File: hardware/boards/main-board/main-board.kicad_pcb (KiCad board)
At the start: 4 copper layers, 292.4 x 42 mm, 159 parts, among them J1 2x12 1.27mm shrouded box head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, J2 1x3, J4 12-way, J5 12-way, J6 8-way 2.54mm right-angle pin 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, Q1 AO3401A, SW1 KS-33, SW2 KS-33, SW3 KS-33, SW4 KS-33, SW5 KS-33, SW6 KS-33, SW7 KS-33, SW8 KS-33, U1 SP0504BAHT or equivalent 4-ch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, U10 MPXV4006DP, U11 SP0504BAHTG 4-channel 5V array, U2 MCP3202-CI/SN, U3 OPA2197IDR, U4 REF5050IDR, U5 R-78E5.0-1.0, U6 74AHCT125, U7 74HCS165, U8 74HCS165, U9 SP0504BAHTG 4-channel 5V array

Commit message: #35 pass 2: values — C1 18nF C0G/NP0, D5/D6 PESD12VL1BA to match the sheets
Owner, 2026-10-04, in the working chat: "Yes, go ahead". Footprints unchanged,
no copper moved; pcb.py check 0 errors (the three parity errors cleared).

Gate-Red: known red, not this commit's: 37 deferred cad outputs, the module-iso coverage row (sim), module-main's kicad check; main-board renders/fab stale until the pass's final render

Co-Authored-By: Claude Opus 5.5 <noreply@anthropic.com>
Claude-Session: https://claude.ai/code/session_01LmB4muFXnoLprWX4JzuJ5A
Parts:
- C1: value 47nF C0G/NP0 -> 18nF C0G/NP0
- D5, D6: value PESD12VS1UA or equivalent 12V-standoff ESD diode -> PESD12VL1BA
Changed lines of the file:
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@@
 			)
 		)
-		(property "Value" "47nF C0G/NP0"
+		(property "Value" "18nF C0G/NP0"
 			(at 0 1.68 90)
 			(layer "F.Fab")
@@
 			)
 		)
-		(property "Value" "PESD12VS1UA or equivalent 12V-standoff ESD diode"
+		(property "Value" "PESD12VL1BA"
 			(at 0.1 1.9 90)
 			(layer "F.Fab")
@@
 			)
 		)
-		(property "Value" "PESD12VS1UA or equivalent 12V-standoff ESD diode"
+		(property "Value" "PESD12VL1BA"
 			(at 0.1 1.9 90)
 			(layer "F.Fab")

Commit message: #35 pass 2: R1–R5 — the five proven single-run fixes
R1 CHAIN_SHLD by J5 13.2 -> 11.2 mm; R2 KEY_LT4 hump flattened 14.3 -> 13.0;
R3 LT3 switch leg north of SW3's hole 13.2 -> 12.2; R4 SCLK one straight run
at y 127.1 under D2; R5 IO36 re-laid with one step each end 168.3 -> 166.1.
The reviewer's proven paths (review35 reroute.json), laid locked. Zones filled;
KiCad DRC 0 unconnected / 0 violations; pcb.py check 0 errors.

Gate-Red: known red, not this commit's: 37 deferred cad outputs, the module-iso coverage row (sim), module-main's kicad check; main-board renders/fab stale until the pass's final render

Co-Authored-By: Claude Opus 5.5 <noreply@anthropic.com>
Claude-Session: https://claude.ai/code/session_01LmB4muFXnoLprWX4JzuJ5A
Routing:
- net /IO36: track 265.1 -> 262.9 mm
- net /CHAIN_SHLD: track 263.1 -> 261.1 mm
- net /KEY_LT4: track 51.4 -> 50.1 mm
- net /LT3/SWITCH_LEG: track 13.2 -> 12.2 mm
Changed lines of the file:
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@@
 	)
 	(segment
-		(start 231.1 108.5)
-		(end 231.1 111.9)
-		(width 0.25)
-		(layer "F.Cu")
-		(net 6)
-	)
-	(segment
 		(start 240.5 112.9)
 		(end 245.1 112.9)
@@
 	)
 	(segment
-		(start 231.1 111.9)
-		(end 231.7 112.5)
+		(start 236.1 108.5)
+		(end 240.5 112.9)
 		(width 0.25)
+		(locked yes)
 		(layer "F.Cu")
 		(net 6)
@@
 	)
 	(segment
-		(start 231.7 112.5)
-		(end 240.1 112.5)
+		(start 231.1 108.5)
+		(end 236.1 108.5)
 		(width 0.25)
+		(locked yes)
 		(layer "F.Cu")
 		(net 6)
@@
 		(net 6)
 	)
-	(segment
-		(start 240.1 112.5)
-		(end 240.5 112.9)
-		(width 0.25)
-		(layer "F.Cu")
-		(net 6)
-	)
 	(via
 		(at 124.7 134.1)
@@
 	)
 	(segment
-		(start 176.3 139.5)
-		(end 180.1 135.7)
+		(start 194.5 135.7)
+		(end 158.3 135.7)
 		(width 0.25)
+		(locked yes)
 		(layer "B.Cu")
 		(net 17)
 	)
 	(segment
-		(start 180.1 135.7)
-		(end 210.5 135.7)
+		(start 113.1 139.5)
+		(end 107.3 133.699999)
 		(width 0.25)
+		(locked yes)
 		(layer "B.Cu")
 		(net 17)
 	)
 	(segment
-		(start 214.3 139.5)
-		(end 246.7 139.5)
+		(start 321.9 136.5)
+		(end 321.9 136.3)
 		(width 0.25)
 		(layer "B.Cu")
@@
 	)
 	(segment
-		(start 321.9 136.5)
-		(end 321.9 136.3)
+		(start 107.3 133.699999)
+		(end 104.1 133.699999)
 		(width 0.25)
+		(locked yes)
 		(layer "B.Cu")
 		(net 17)
 	)
 	(segment
-		(start 105.1 134.7)
-		(end 105.1 138.3)
+		(start 154.5 139.5)
+		(end 113.1 139.5)
 		(width 0.25)
+		(locked yes)
 		(layer "B.Cu")
 		(net 17)
 	)
 	(segment
-		(start 105.1 138.3)
-		(end 106.3 139.5)
+		(start 252.1 134.1)
+		(end 247.7 138.5)
 		(width 0.25)
+		(locked yes)
 		(layer "B.Cu")
 		(net 17)
 	)
 	(segment
-		(start 254.9 131.3)
-		(end 254.9 129.9)
+		(start 252.1 132.699999)
+		(end 252.1 134.1)
 		(width 0.25)
+		(locked yes)
 		(layer "B.Cu")
 		(net 17)
 	)
 	(segment
-		(start 106.3 139.5)
-		(end 176.3 139.5)
+		(start 158.3 135.7)
+		(end 154.5 139.5)
 		(width 0.25)
+		(locked yes)
 		(layer "B.Cu")
 		(net 17)
 	)
 	(segment
-		(start 254.9 129.9)
-		(end 258.5 126.3)
+		(start 247.7 138.5)
+		(end 220.1 138.5)
 		(width 0.25)
+		(locked yes)
 		(layer "B.Cu")
 		(net 17)
 	)
 	(segment
-		(start 210.5 135.7)
-		(end 214.3 139.5)
+		(start 258.5 126.3)
+		(end 252.1 132.699999)
 		(width 0.25)
+		(locked yes)
 		(layer "B.Cu")
 		(net 17)
 	)
 	(segment
-		(start 323.5 134.7)
-		(end 334.9 134.7)
+		(start 220.1 138.5)
+		(end 216.5 134.9)
 		(width 0.25)
+		(locked yes)
 		(layer "B.Cu")
 		(net 17)
 	)
 	(segment
-		(start 319.7 126.3)
-		(end 319.7 129.9)
+		(start 216.5 134.9)
+		(end 195.3 134.9)
 		(width 0.25)
+		(locked yes)
 		(layer "B.Cu")
 		(net 17)
 	)
 	(segment
-		(start 104.1 133.699999)
-		(end 105.1 134.7)
+		(start 323.5 134.7)
+		(end 334.9 134.7)
+		(width 0.25)
+		(layer "B.Cu")
+		(net 17)
+	)
+	(segment
+		(start 319.7 126.3)
+		(end 319.7 129.9)
 		(width 0.25)
 		(layer "B.Cu")
@@
 	)
 	(segment
-		(start 246.7 139.5)
-		(end 254.9 131.3)
+		(start 195.3 134.9)
+		(end 194.5 135.7)
 		(width 0.25)
+		(locked yes)
 		(layer "B.Cu")
 		(net 17)
@@
 	)
 	(segment
-		(start 150.1 106.7)
-		(end 149.1 106.7)
+		(start 151.5 108.3)
+		(end 147.5 108.3)
 		(width 0.25)
+		(locked yes)
 		(layer "B.Cu")
 		(net 26)
 	)
 	(segment
-		(start 155.3 111.9)
-		(end 150.1 106.7)
+		(start 155.9 111.9)
+		(end 155.1 111.9)
 		(width 0.25)
+		(locked yes)
 		(layer "B.Cu")
 		(net 26)
 	)
 	(segment
-		(start 155.9 111.9)
-		(end 155.3 111.9)
+		(start 155.1 111.9)
+		(end 151.5 108.3)
 		(width 0.25)
+		(locked yes)
 		(layer "B.Cu")
 		(net 26)
 	)
 	(segment
-		(start 139.9 113.9)
-		(end 137.1 116.7)
+		(start 147.5 108.3)
+		(end 145.3 110.5)
 		(width 0.25)
+		(locked yes)
 		(layer "B.Cu")
 		(net 26)
 	)
 	(segment
-		(start 149.1 106.7)
-		(end 145.3 110.5)
+		(start 139.9 113.9)
+		(end 137.1 116.7)
 		(width 0.25)
 		(layer "B.Cu")
@@
 	)
 	(segment
-		(start 145.299999 139.5)
-		(end 150.3 139.5)
+		(start 150.9 134.9)
+		(end 152.9 136.9)
 		(width 0.25)
+		(locked yes)
 		(layer "F.Cu")
 		(net 35)
 	)
 	(segment
-		(start 142.1 136.3)
-		(end 145.299999 139.5)
+		(start 144.9 136.3)
+		(end 146.3 134.9)
 		(width 0.25)
+		(locked yes)
 		(layer "F.Cu")
 		(net 35)
 	)
 	(segment
-		(start 150.3 139.5)
-		(end 152.9 136.9)
+		(start 146.3 134.9)
+		(end 150.9 134.9)
 		(width 0.25)
+		(locked yes)
+		(layer "F.Cu")
+		(net 35)
+	)
+	(segment
+		(start 142.1 136.3)
+		(end 144.9 136.3)
+		(width 0.25)
+		(locked yes)
 		(layer "F.Cu")
 		(net 35)
@@
 	)
 	(segment
-		(start 336.9 126.7)
-		(end 345.5 126.7)
+		(start 354.9 127.1)
+		(end 338.1 127.1)
 		(width 0.25)
+		(locked yes)
 		(layer "B.Cu")
 		(net 42)
 	)
 	(segment
-		(start 345.9 127.1)
-		(end 354.9 127.1)
+		(start 336.9 126.7)
+		(end 335.5 128.1)
 		(width 0.25)
+		(locked yes)
 		(layer "B.Cu")
 		(net 42)
 	)
 	(segment
-		(start 345.5 126.7)
-		(end 345.9 127.1)
+		(start 337.7 126.7)
+		(end 336.9 126.7)
 		(width 0.25)
+		(locked yes)
 		(layer "B.Cu")
 		(net 42)
 	)
 	(segment
-		(start 335.5 128.1)
-		(end 336.9 126.7)
+		(start 338.1 127.1)
+		(end 337.7 126.7)
 		(width 0.25)
+		(locked yes)
 		(layer "B.Cu")
 		(net 42)

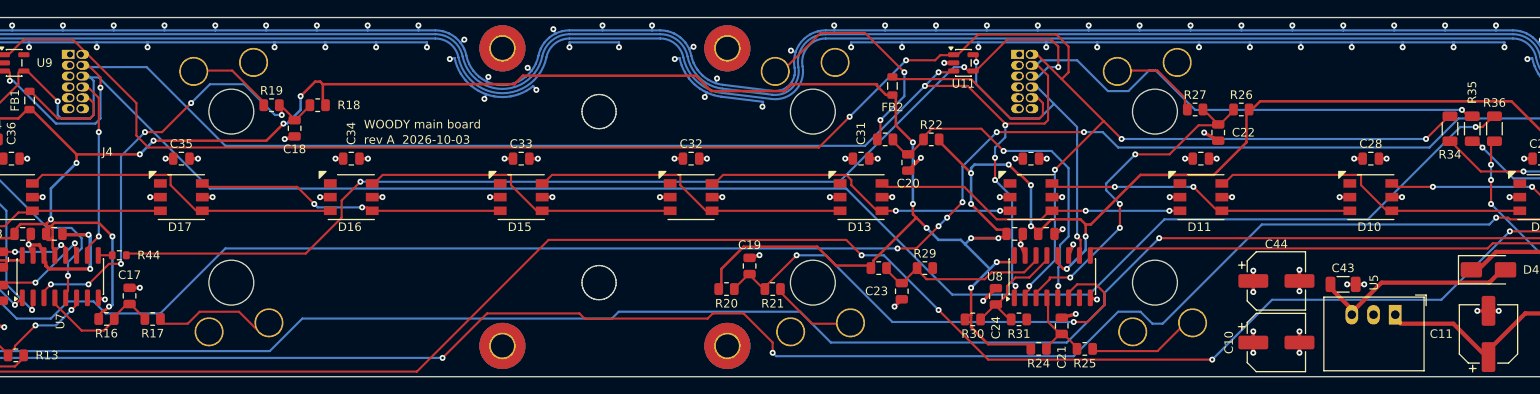
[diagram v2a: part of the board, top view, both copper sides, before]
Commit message: #35 pass 2: R11 WIP — U8/J5 fan-in re-laid (82 -> 72 vias on 14 nets), joins not yet clean
Checkpoint (container restarts). 14 nets re-laid in the U8/J5 box in one pass,
DEV_3V3 first on F, then key lines, chain, IO bus; all new copper locked.
KiCad DRC: 0 unconnected, 0 violations. pcb.py check: 6 errors still to fix
in the next commit (one 0.04 mm dangling stub, five acute joins at cut ends).

Gate-Red: WIP: pcb.py check main-board 6 errors (tracks acid traps, 1 dangling stub) fixed next commit; known red: 37 deferred cad outputs, the module-iso coverage row (sim), module-main's kicad check; main-board renders/fab stale until the final render

Co-Authored-By: Claude Opus 5.5 <noreply@anthropic.com>
Claude-Session: https://claude.ai/code/session_01LmB4muFXnoLprWX4JzuJ5A
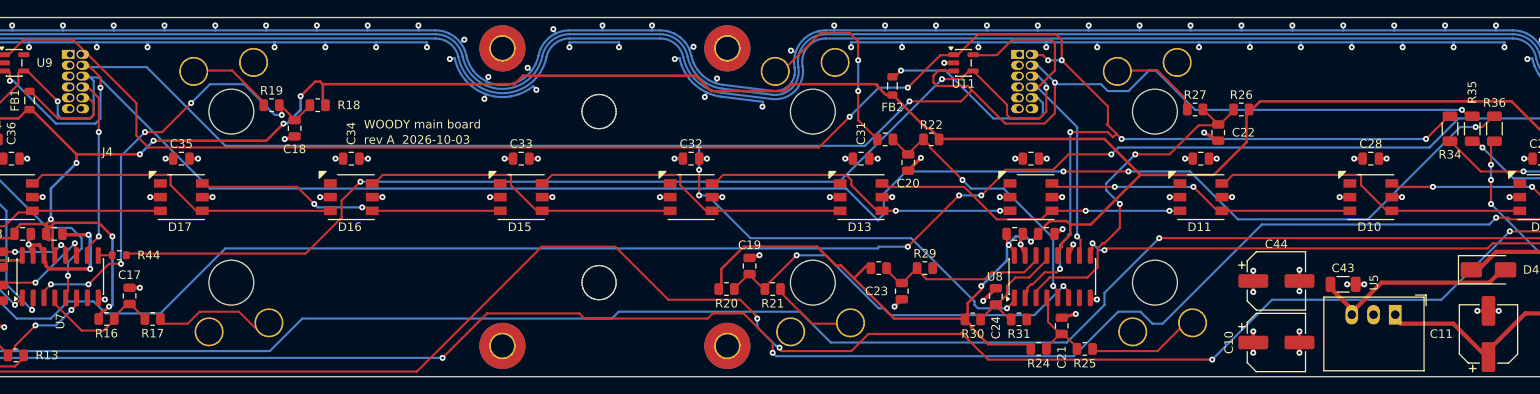
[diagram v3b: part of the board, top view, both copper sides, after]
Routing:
- net /CHAIN_SHLD: track 261.1 -> 291.9 mm, vias 11 -> 10
- net DEV_3V3: track 498.0 -> 483.8 mm, vias 27 -> 16
- net /KEY_RT1: track 53.8 -> 44.8 mm
- net /CHAIN_SCK: track 250.5 -> 255.7 mm, vias 8 -> 10
- net /HOP_RH_RT: track 35.5 -> 40.1 mm, vias 2 -> 1
- net /KEY_RT2: track 36.2 -> 32.4 mm
- net /IO39: track 260.9 -> 257.1 mm, vias 10 -> 8
- net /RT2/SWITCH_LEG: track 25.4 -> 22.6 mm
- net /KEY_RT4: track 36.7 -> 38.8 mm, vias 4 -> 2
- net /V3V3_CHAIN_RH: track 21.5 -> 23.5 mm, vias 0 -> 1
- net /IO35: track 276.8 -> 278.8 mm
- net /CHAIN_QH_RT: track 83.9 -> 85.8 mm, vias 2 -> 4
- net /HOP_LT_RH: track 124.8 -> 126.2 mm
- net /CHAIN_SER_LH: track 203.6 -> 202.5 mm, vias 2 -> 4

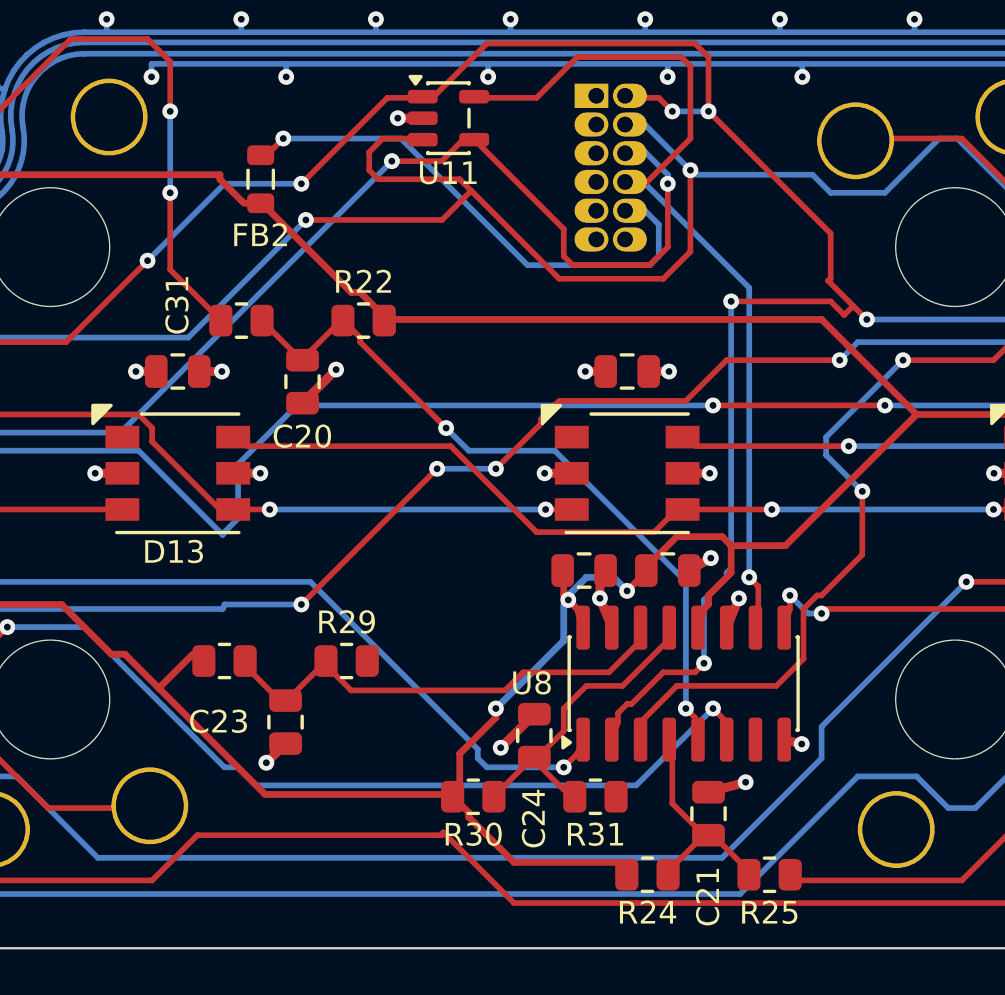
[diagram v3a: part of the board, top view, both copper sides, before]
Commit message: #35 pass 2: R11 (R6–R10, R13 nets, R21) — U8/J5 fan-in re-laid, joins squared
14 nets re-laid together in the U8/J5 box (226,103 - 252,137): DEV_3V3 first,
preferring F, then KEY_RT1/RT2/RT4 and the RT2 leg, the J5/U11 chain (HOP_RH_RT,
HOP_LT_RH, CHAIN_SHLD, CHAIN_SCK, V3V3_CHAIN_RH), CHAIN_QH_RT, CHAIN_SER_LH,
then the IO bus (IO39, IO35); A* on the board's own obstacle model, via cost 60
grid steps, string-pulled to straight and 45-degree runs, all locked. Vias on
those nets 82 -> 72 (board signal vias 148 -> 138), 0 unconnected. The mid-run
via of R21 is gone with DEV_3V3's re-lay. Six joins the re-lay left acute or
doubled squared by hand; pcb_route.tidy run with its locked-via trap guarded.
DRC 0/0; pcb.py check 0 errors.

Gate-Red: known red, not this commit's: 37 deferred cad outputs, the module-iso coverage row (sim), module-main's kicad check; main-board renders/fab stale until the final render

Co-Authored-By: Claude Opus 5.5 <noreply@anthropic.com>
Claude-Session: https://claude.ai/code/session_01LmB4muFXnoLprWX4JzuJ5A
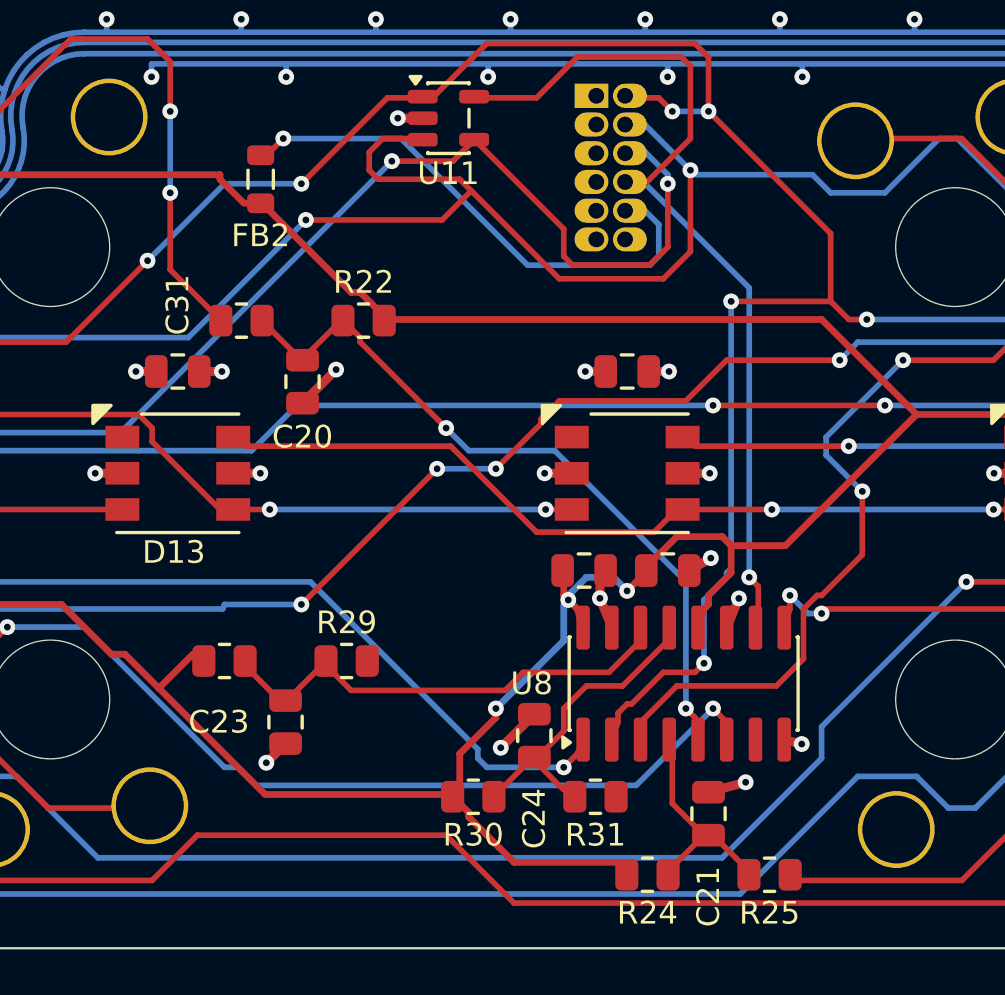
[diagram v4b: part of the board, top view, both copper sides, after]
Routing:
- net /CHAIN_SER_LH: track 202.5 -> 198.0 mm
- net /CHAIN_SCK: track 255.7 -> 254.6 mm
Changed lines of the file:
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@@
 	)
 	(segment
-		(start 243.1 132.1)
-		(end 243.1 132.5)
+		(start 252.5 113.9)
+		(end 253.3 114.7)
 		(width 0.25)
 		(locked yes)
@@
 	)
 	(segment
-		(start 252.375 112.975)
-		(end 252.4 113)
+		(start 243.1 132.1)
+		(end 243.1 132.5)
 		(width 0.25)
 		(locked yes)
@@
 	)
 	(segment
-		(start 243.1 132.5)
-		(end 242.825 133.275)
+		(start 253.3 114.7)
+		(end 254.1 114.7)
 		(width 0.25)
 		(locked yes)
@@
 	)
 	(segment
-		(start 138.9 110.5)
-		(end 138.9 114.3)
+		(start 243.1 132.5)
+		(end 242.825 133.275)
 		(width 0.25)
+		(locked yes)
 		(layer "F.Cu")
 		(net 4)
 	)
 	(segment
-		(start 252.5 112.9)
-		(end 252.4 113)
+		(start 138.9 110.5)
+		(end 138.9 114.3)
 		(width 0.25)
-		(locked yes)
 		(layer "F.Cu")
 		(net 4)
@@
 	)
 	(segment
-		(start 252.4 113)
-		(end 253.5 114.1)
-		(width 0.25)
-		(locked yes)
-		(layer "F.Cu")
-		(net 4)
-	)
-	(segment
-		(start 253.5 114.1)
-		(end 254.1 114.7)
-		(width 0.25)
-		(locked yes)
-		(layer "F.Cu")
-		(net 4)
-	)
-	(segment
 		(start 243.5 104.9)
 		(end 244.9 104.9)
@@
 	(segment
 		(start 252.5 110.9)
-		(end 252.5 112.9)
+		(end 252.5 113.9)
 		(width 0.25)
 		(locked yes)
@@
 	)
 	(segment
-		(start 253.1 114.5)
-		(end 252.5 113.9)
-		(width 0.25)
-		(locked yes)
-		(layer "F.Cu")
-		(net 4)
-	)
-	(segment
 		(start 234.5 104.9)
 		(end 234.9 104.9)
@@
 	)
 	(segment
-		(start 253.5 114.1)
-		(end 253.1 114.5)
-		(width 0.25)
-		(locked yes)
-		(layer "F.Cu")
-		(net 4)
-	)
-	(segment
 		(start 122.9 104.9)
 		(end 121.9 104.9)
@@
 	)
 	(segment
-		(start 221.9 120.5)
-		(end 225.625 124.225)
-		(width 0.25)
-		(locked yes)
-		(layer "B.Cu")
-		(net 5)
-	)
-	(segment
 		(start 254.9 118.5)
 		(end 262.1 118.5)
@@
 	)
 	(segment
+		(start 226.9 120.5)
+		(end 228.9 118.5)
+		(width 0.25)
+		(locked yes)
+		(layer "B.Cu")
+		(net 5)
+	)
+	(segment
 		(start 129.699999 111.9)
 		(end 130.1 112.3)
@@
 	)
 	(segment
-		(start 226.3 123.5)
-		(end 226.3 121.1)
-		(width 0.25)
-		(locked yes)
-		(layer "B.Cu")
-		(net 5)
-	)
-	(segment
-		(start 225.625 124.225)
-		(end 225.7 124.1)
-		(width 0.25)
-		(locked yes)
-		(layer "B.Cu")
-		(net 5)
-	)
-	(segment
 		(start 147.5 120.5)
 		(end 221.9 120.5)
@@
 	)
 	(segment
-		(start 226.3 121.1)
-		(end 228.9 118.5)
-		(width 0.25)
-		(locked yes)
-		(layer "B.Cu")
-		(net 5)
-	)
-	(segment
-		(start 225.7 124.1)
-		(end 226.3 123.5)
+		(start 133.9 107.9)
+		(end 133.3 107.3)
 		(width 0.25)
-		(locked yes)
 		(layer "B.Cu")
 		(net 5)
 	)
 	(segment
-		(start 133.9 107.9)
-		(end 133.3 107.3)
+		(start 133.3 107.5)
+		(end 134.5 107.5)
 		(width 0.25)
 		(layer "B.Cu")
@@
 	)
 	(segment
-		(start 133.3 107.5)
-		(end 134.5 107.5)
+		(start 221.9 120.5)
+		(end 226.9 120.5)
 		(width 0.25)
+		(locked yes)
 		(layer "B.Cu")
 		(net 5)
@@
 	)
 	(segment
+		(start 235.8 107.7)
+		(end 233.1 107.7)
+		(width 0.25)
+		(locked yes)
+		(layer "F.Cu")
+		(net 11)
+	)
+	(segment
 		(start 162.9 123.9)
 		(end 158.7 128.1)
@@
 	)
 	(segment
-		(start 236.7375 106.75)
-		(end 236.7 106.7)
-		(width 0.25)
-		(locked yes)
-		(layer "F.Cu")
-		(net 11)
-	)
-	(segment
 		(start 241.1 112.3)
 		(end 244.5 112.3)
@@
 	)
 	(segment
-		(start 236.3 106.7)
-		(end 235.3 107.7)
-		(width 0.25)
-		(locked yes)
-		(layer "F.Cu")
-		(net 11)
-	)
-	(segment
 		(start 158.7 128.1)
 		(end 138.1 128.1)
@@
 	)
 	(segment
-		(start 235.3 107.7)
-		(end 233.1 107.7)
-		(width 0.25)
-		(locked yes)
-		(layer "F.Cu")
-		(net 11)
-	)
-	(segment
 		(start 162.9 121.9)
 		(end 162.9 123.9)
@@
 	)
 	(segment
-		(start 236.7 106.7)
+		(start 236.75 106.75)
 		(end 240.7 110.7)
 		(width 0.25)
@@
 	)
 	(segment
-		(start 236.7 106.7)
-		(end 236.3 106.7)
+		(start 236.75 106.75)
+		(end 235.8 107.7)
 		(width 0.25)
 		(locked yes)
@@
 	)
 	(segment
-		(start 235.375 137.375)
-		(end 235.3 137.5)
-		(width 0.25)
-		(locked yes)
-		(layer "F.Cu")
-		(net 16)
-	)
-	(segment
 		(start 194.9 127.3)
 		(end 186.3 127.3)
@@
 	)
 	(segment
-		(start 235.375 137.375)
+		(start 235.5 137.5)
 		(end 238.5 140.5)
 		(width 0.25)
@@
 	)
 	(segment
-		(start 235.3 137.5)
+		(start 235.5 137.5)
 		(end 224.5 137.5)
 		(width 0.25)
@@
 	)
 	(segment
-		(start 230.9375 114.75)
-		(end 230.9 114.7)
-		(width 0.25)
-		(locked yes)
-		(layer "F.Cu")
-		(net 28)
-	)
-	(segment
 		(start 230.9 114.7)
 		(end 231.7 115.5)
@@
 	(segment
 		(start 231.7 113.5)
-		(end 232.5 114.3)
+		(end 232.7 114.5)
 		(width 0.3)
 		(locked yes)
@@
 	)
 	(segment
-		(start 232.5 114.3)
-		(end 232.7625 114.75)
-		(width 0.3)
-		(locked yes)
-		(layer "F.Cu")
-		(net 80)
-	)
-	(segment
 		(start 122.7 112.3)
 		(end 122.7 114.1)
@@
 	)
 	(segment
+		(start 232.7 114.5)
+		(end 232.7 114.7)
+		(width 0.3)
+		(locked yes)
+		(layer "F.Cu")
+		(net 80)
+	)
+	(segment
 		(start 306.7 117.3)
 		(end 305.1 118.9)
@@
 		(layer "F.Cu")
 		(net 80)
-	)
-	(segment
-		(start 232.7625 114.75)
-		(end 232.7 114.7)
-		(width 0.3)
-		(locked yes)
-		(layer "F.Cu")
-		(net 80)

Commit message: #35 pass 2: R11 polish — seven runs re-searched to fewer bends
IO39 B 10 -> 4 bends, IO35 F 5 -> 1, CHAIN_SHLD (two runs), DEV_3V3, KEY_RT2,
CHAIN_SCK one fewer each; same ends and layer, string-pulled, locked.
DRC 0/0; pcb.py check 0 errors.

Gate-Red: known red, not this commit's: 37 deferred cad outputs, the module-iso coverage row (sim), module-main's kicad check; main-board renders/fab stale until the final render

Co-Authored-By: Claude Opus 5.5 <noreply@anthropic.com>
Claude-Session: https://claude.ai/code/session_01LmB4muFXnoLprWX4JzuJ5A
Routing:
- net /IO35: track 278.6 -> 277.0 mm
- net /CHAIN_SHLD: track 291.9 -> 290.5 mm

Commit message: #35 pass 2: R11 — CHAIN_SHLD's U8.1 branch re-laid nearer (290.5 -> 272.7 mm)
The group re-lay had joined U8.1 to SHLD from x 204.7 (40 mm, two extra
vias); taken up and routed again from the nearest SHLD copper. DRC 0/0;
pcb.py check 0 errors.

Gate-Red: known red, not this commit's: 37 deferred cad outputs, the module-iso coverage row (sim), module-main's kicad check; main-board renders/fab stale until the final render

Co-Authored-By: Claude Opus 5.5 <noreply@anthropic.com>
Claude-Session: https://claude.ai/code/session_01LmB4muFXnoLprWX4JzuJ5A
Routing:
- net /CHAIN_SHLD: track 290.5 -> 272.7 mm
